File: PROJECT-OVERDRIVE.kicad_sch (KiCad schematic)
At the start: 57 parts, among them J1 PJ-327A0-SMT, J2 USB_C_Receptacle_USB2.0_16P, K1 G6S-2, P1 SSD1306_ribbon, U1 CH32V30xVxTx, U2 PCM5102APWR, U3 MAX4410EUD+, U4 AP2112K-3.3, U5 AP2112K-3.3, U6 LM324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

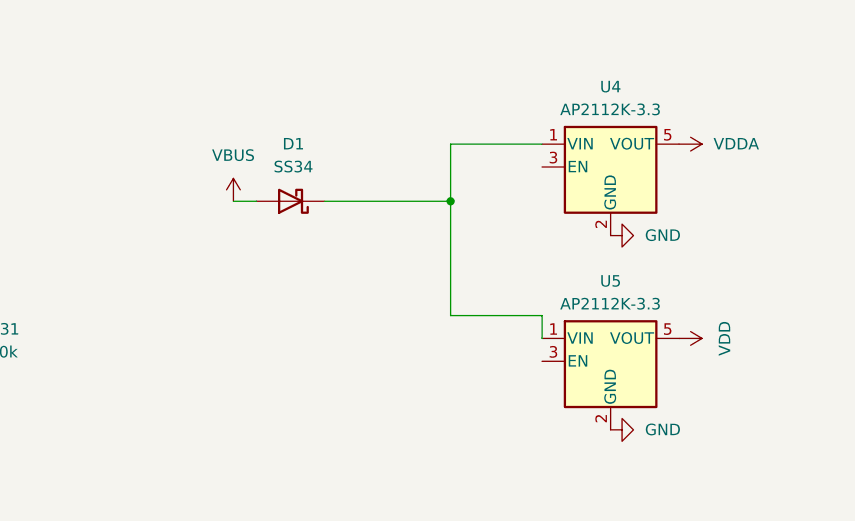
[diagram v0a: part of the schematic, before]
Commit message: Add fuses
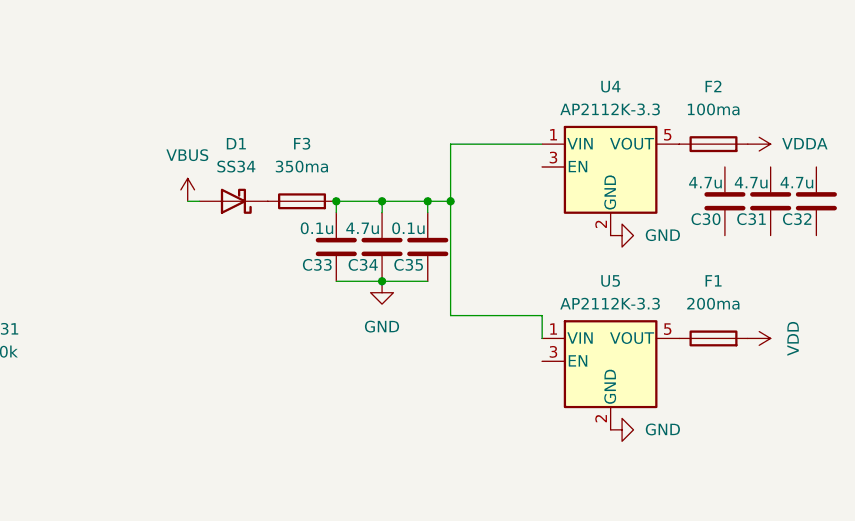
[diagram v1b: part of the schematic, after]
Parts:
- added C30, C31, C32, C34: 4.7u, Capacitor_SMD:C_0805_2012Metric, symbol Device:C
- added C33, C35: 0.1u, Capacitor_SMD:C_0805_2012Metric, symbol Device:C
- added F1: 200ma, Fuse:Fuse_0805_2012Metric, symbol Device:Fuse
- added F2: 100ma, Fuse:Fuse_0805_2012Metric, symbol Device:Fuse
- added F3: 350ma, Fuse:Fuse_0805_2012Metric, symbol Device:Fuse
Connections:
- net GND: now also C33.2, C34.2, C35.2
- net VDD: now also F1.2; no longer U5.5 (VOUT)
- net VDDA: now also F2.2; no longer U4.5 (VOUT)
- net at U4.1 (VIN), U5.1 (VIN): now also C33.1, C34.1, C35.1, F3.2; no longer D1.1 (K)
- new net: F2.1, U4.5 (VOUT)
- new net: D1.1 (K), F3.1
- new net: F1.1, U5.5 (VOUT)
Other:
- moved on the sheet: D1

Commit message: finished power supply section
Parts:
- added C36, C37: 4.7u, Capacitor_SMD:C_0805_2012Metric, symbol Device:C
- added C38: 0.1u, Capacitor_SMD:C_0805_2012Metric, symbol Device:C
- added Q1, Q2: AO3401A, Package_TO_SOT_SMD:SOT-23, symbol Transistor_FET:AO3401A
- added R10, R9: 1k, Resistor_SMD:R_0805_2012Metric_Pad1.20x1.40mm_HandSolder, symbol Device:R
- added R11, R12: 10k, Resistor_SMD:R_0805_2012Metric_Pad1.20x1.40mm_HandSolder, symbol Device:R
- C32: value 4.7u -> 0.1u
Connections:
- net +3.3VA: now also Q2.3 (D); no longer U6.3 (+), U6.5 (+)
- net +3.3VDAC: now also Q1.3 (D)
- net GND: now also C30.2, C31.2, C32.2, C36.2, C37.2, C38.2
- net VDDA: now also U6.3 (+), U6.5 (+), Q1.2 (S), Q2.2 (S), R11.2, R12.2
- net at F2.1, U4.5 (VOUT): now also C30.1, C31.1, C32.1
- net at F1.1, U5.5 (VOUT): now also C36.1, C37.1, C38.1
- new net: Q2.1 (G), R10.2, R11.1
- new net: Q1.1 (G), R12.1, R9.2
- new net VAMP_EN: R10.1
- new net VDAC_EN: R9.1
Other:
- note added: "POWER"

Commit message: added exp port(to be finished)
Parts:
- added F4: 250ma, Fuse:Fuse_0805_2012Metric, symbol Device:Fuse
- added J3: Conn_02x10_Odd_Even, symbol Connector_Generic:Conn_02x10_Odd_Even
- added Q3: S8050, Package_TO_SOT_THT:TO-92_Inline, symbol Transistor_BJT:S8050
- added RN1, RN2: 22, Resistor_SMD:R_Array_Concave_4x0603, symbol Device:R_Pack04
- F3: value 350ma -> 250ma
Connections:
- net DAC_BCK: now also RN1.8 (R1.2)
- net DAC_MUTE: now also U1.53 (PB14)
- net GND: now also Q3.1 (E)
- net +5V: now reaches K1.1
- net +5V: now also C33.1, C34.1, C35.1, F3.2, U4.1 (VIN), U5.1 (VIN)
- net at K1.12: now also Q3.3 (C)
- net at D1.1 (K), F3.1: now also F4.2
- net EXP_I2S_LRCLK: now reaches U1.77 (PA15)
- net EXP_I2S_LRCLK: now also RN1.7 (R2.2)
- net EXP_I2S_CLK: now reaches U1.89 (PB3)
- net EXP_I2S_CLK: now also RN1.6 (R3.2)
- net EXP_I2S_SD: now reaches U1.91 (PB5)
- net EXP_I2S_SD: now also RN1.5 (R4.2)
- new net: J3.10 (Pin_10), RN2.8 (R1.2)
- new net: J3.3 (Pin_3), RN1.4 (R4.1)
- new net: J3.4 (Pin_4), RN2.5 (R4.2)
- new net: J3.5 (Pin_5), RN1.3 (R3.1)
- new net: J3.6 (Pin_6), RN2.6 (R3.2)
- new net: J3.7 (Pin_7), RN1.2 (R2.1)
- new net: J3.8 (Pin_8), RN2.7 (R2.2)
- new net: J3.9 (Pin_9), RN1.1 (R1.1)
- new net +5VP: F4.1

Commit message: expansion port mostly finished(TODO:Add some gpios to there) relay circuit finished(need to connect to mcu)
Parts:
- removed RN1: 22, Resistor_SMD:R_Array_Concave_4x0603, symbol Device:R_Pack04
- added R13, R14, R15: 22r, Resistor_SMD:R_0603_1608Metric, symbol Device:R
- added R16: 1k, Resistor_SMD:R_0805_2012Metric, symbol Device:R
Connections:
- net +5VP: now also J3.1 (Pin_1), J3.2 (Pin_2)
- net DAC_BCK: now also J3.6 (Pin_6), RN2.6 (R3.2); no longer U1.52 (PB13), U2.13 (BCK)
- net DAC_DIN: now also J3.4 (Pin_4), RN2.8 (R1.2); no longer U1.54 (PB15), U2.14 (DIN)
- net DAC_LRCLK: now also J3.8 (Pin_8), RN2.5 (R4.2); no longer U1.51 (PB12), U2.15 (LRCK)
- net DAC_MUTE: now also J3.10 (Pin_10), RN2.7 (R2.2); no longer U1.53 (PB14)
- net EXP_I2S_CLK: now also J3.5 (Pin_5), R14.1; no longer U1.89 (PB3)
- net EXP_I2S_LRCLK: now also J3.7 (Pin_7), R13.1; no longer U1.77 (PA15)
- net EXP_I2S_SD: now also J3.3 (Pin_3), R15.1; no longer U1.91 (PB5)
- net GND: now also J3.19 (Pin_19), J3.20 (Pin_20)
- net I2C_SCL: now reaches J3.15 (Pin_15)
- net I2C_SCL: now also U1.47 (PB10)
- net I2C_SDA: now reaches J3.17 (Pin_17)
- net I2C_SDA: now also U1.48 (PB11)
- net at RN2.1 (R1.1): now also U1.54 (PB15)
- net at RN2.2 (R2.1): now also U1.53 (PB14)
- net at RN2.3 (R3.1): now also U1.52 (PB13)
- net at RN2.4 (R4.1): now also U1.51 (PB12)
- net at Q3.2 (B): now also R16.2
- new net: R13.2, U1.77 (PA15)
- new net: R14.2, U1.89 (PB3)
- new net: R15.2, U1.91 (PB5)
- new net RELAY_TOGGLE: R16.1
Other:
- moved on the sheet: RN2

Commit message: idkmyinternetwasdead.git
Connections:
- net DAC_BCK: now also U2.13 (BCK)
- net DAC_DIN: now also U2.14 (DIN)
- net DAC_LRCLK: now also U2.15 (LRCK)
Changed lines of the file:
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@@
 	(global_label "DAC_LRCLK"
 		(shape input)
-		(at 170.561 91.059 270)
-		(fields_autoplaced yes)
-		(effects
-			(font
-				(size 1.27 1.27)
-			)
-			(justify right)
-		)
-		(property "Intersheetrefs" "${INTERSHEET_REFS}"
-			(at 170.561 104.5066 90)
+		(at 166.37 95.25 180)
+		(fields_autoplaced yes)
+		(effects
+			(font
+				(size 1.27 1.27)
+			)
+			(justify right)
+		)
+		(property "Intersheetrefs" "${INTERSHEET_REFS}"
+			(at 152.9224 95.25 0)
 			(effects
 				(font
@@
 	(global_label "DAC_DIN"
 		(shape input)
-		(at 162.941 91.059 270)
-		(fields_autoplaced yes)
-		(effects
-			(font
-				(size 1.27 1.27)
-			)
-			(justify right)
-		)
-		(property "Intersheetrefs" "${INTERSHEET_REFS}"
-			(at 162.941 101.8457 90)
+		(at 166.37 87.63 180)
+		(fields_autoplaced yes)
+		(effects
+			(font
+				(size 1.27 1.27)
+			)
+			(justify right)
+		)
+		(property "Intersheetrefs" "${INTERSHEET_REFS}"
+			(at 155.5833 87.63 0)
 			(effects
 				(font
@@
 	(global_label "DAC_BCK"
 		(shape input)
-		(at 165.481 91.059 270)
-		(fields_autoplaced yes)
-		(effects
-			(font
-				(size 1.27 1.27)
-			)
-			(justify right)
-		)
-		(property "Intersheetrefs" "${INTERSHEET_REFS}"
-			(at 165.481 102.4504 90)
-			(effects
-				(font
+		(at 166.37 90.17 180)
+		(fields_autoplaced yes)
+		(effects
+			(font
+				(size 1.27 1.27)
+			)
+			(justify right)
+		)
+		(property "Intersheetrefs" "${INTERSHEET_REFS}"
+			(at 154.9786 90.17 0)
+			(effects
+				(font

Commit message: fixed up op amp connection
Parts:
- added R17, R18, R19: 10k, Resistor_SMD:R_0805_2012Metric, symbol Device:R
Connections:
- net GND: now also R18.1
- net VDDA: now also R17.1, R19.2; no longer U6.3 (+)
- net at J1.6, U6.2 (-): now also R19.1
- new net: R17.2, R18.2, U6.3 (+)

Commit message: idk
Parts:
- added R20: 100k, Resistor_SMD:R_0805_2012Metric, symbol Device:R
- R19: value 10k -> 100k
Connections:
- net at J1.6, R19.1: now also R20.2; no longer U6.2 (-)
- new net: R20.1, U6.2 (-)
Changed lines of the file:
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@@
 	)
 	(junction
+		(at 259.08 119.38)
+		(diameter 0)
+		(color 0 0 0 0)
+	)
+	(junction
 		(at 248.92 52.324)
 		(diameter 0)
@@
 	)
 	(junction
-		(at 259.08 119.38)
-		(diameter 0)
-		(color 0 0 0 0)
-	)
-	(junction
 		(at 142.24 30.48)
 		(diameter 0)
@@
 	(wire
 		(pts
-			(xy 259.08 132.08) (xy 256.54 132.08)
+			(xy 60.96 193.04) (xy 68.58 193.04)
 		)
 		(stroke
 			(width 0)
 			(type default)
-			(color 255 255 0 1)
 		)
 	)
 	(wire
 		(pts
-			(xy 60.96 193.04) (xy 68.58 193.04)
+			(xy 43.18 24.13) (xy 48.26 24.13)
 		)
 		(stroke
@@
 	(wire
 		(pts
-			(xy 43.18 24.13) (xy 48.26 24.13)
+			(xy 63.5 31.75) (xy 68.58 31.75)
 		)
 		(stroke
@@
 	(wire
 		(pts
-			(xy 63.5 31.75) (xy 68.58 31.75)
+			(xy 340.36 34.29) (xy 345.44 34.29)
 		)
 		(stroke
@@
 	(wire
 		(pts
-			(xy 340.36 34.29) (xy 345.44 34.29)
+			(xy 250.952 49.784) (xy 249.936 49.784)
 		)
 		(stroke
@@
 	(wire
 		(pts
-			(xy 250.952 49.784) (xy 249.936 49.784)
+			(xy 259.08 119.38) (xy 259.08 124.46)
 		)
 		(stroke
@@
 	(wire
 		(pts
+			(xy 259.08 132.08) (xy 256.54 132.08)
+		)
+		(stroke
+			(width 0)
+			(type default)
+			(color 255 255 0 1)
+		)
+	)
+	(wire
+		(pts
 			(xy 85.09 40.64) (xy 85.09 41.91)
 		)
@@
 	(wire
 		(pts
-			(xy 259.08 119.38) (xy 259.08 132.08)
-		)
-		(stroke
-			(width 0)
-			(type default)
-			(color 255 255 0 1)
-		)
-	)
-	(wire
-		(pts
 			(xy 246.38 95.25) (xy 238.76 95.25)
 		)
@@
 		(dnp no)
 		(property "Reference" "R18"
-			(at 261.62 128.778 90)
+			(at 265.176 125.222 90)
 			(effects
 				(font
@@
 			)
 		)
-		(property "Value" "10k"
+		(property "Value" "100k"
 			(at 267.97 115.57 90)
 			(effects
@@
 					(unit 1)
 				)
+			)
+		)
+	)
+	(symbol
+		(lib_id "Device:R")
+		(at 259.08 128.27 180)
+		(unit 1)
+		(exclude_from_sim no)
+		(in_bom yes)
+		(on_board yes)
+		(dnp no)
+		(property "Reference" "R20"
+			(at 256.794 133.096 0)
+			(effects
+				(font
+					(size 1.27 1.27)
+				)
+				(justify right)
+			)
+		)
+		(property "Value" "100k"
+			(at 260.604 130.048 0)
+			(effects
+				(font
+					(size 1.27 1.27)
+				)
+				(justify right)
+			)
+		)
+		(property "Footprint" "Resistor_SMD:R_0805_2012Metric"
+			(at 260.858 128.27 90)
+			(effects
+				(font
+					(size 1.27 1.27)
+				)
+				(hide yes)
+			)
+		)
+		(property "Datasheet" "~"
+			(at 259.08 128.27 0)
+			(effects
+				(font
+					(size 1.27 1.27)
+				)
+				(hide yes)
+			)
+		)
+		(property "Description" "Resistor"
+			(at 259.08 128.27 0)
+			(effects
+				(font
+					(size 1.27 1.27)
+				)
+				(hide yes)
+			)
+		)
+		(pin "2"
+		)
+		(pin "1"
+		)
+		(instances
+			(project "PROJECT-OVERDRIVE"
+				(path "/265f6b68-58df-43b8-965c-fef7b735041c"
+					(reference "R20")
+					(unit 1)
+				)

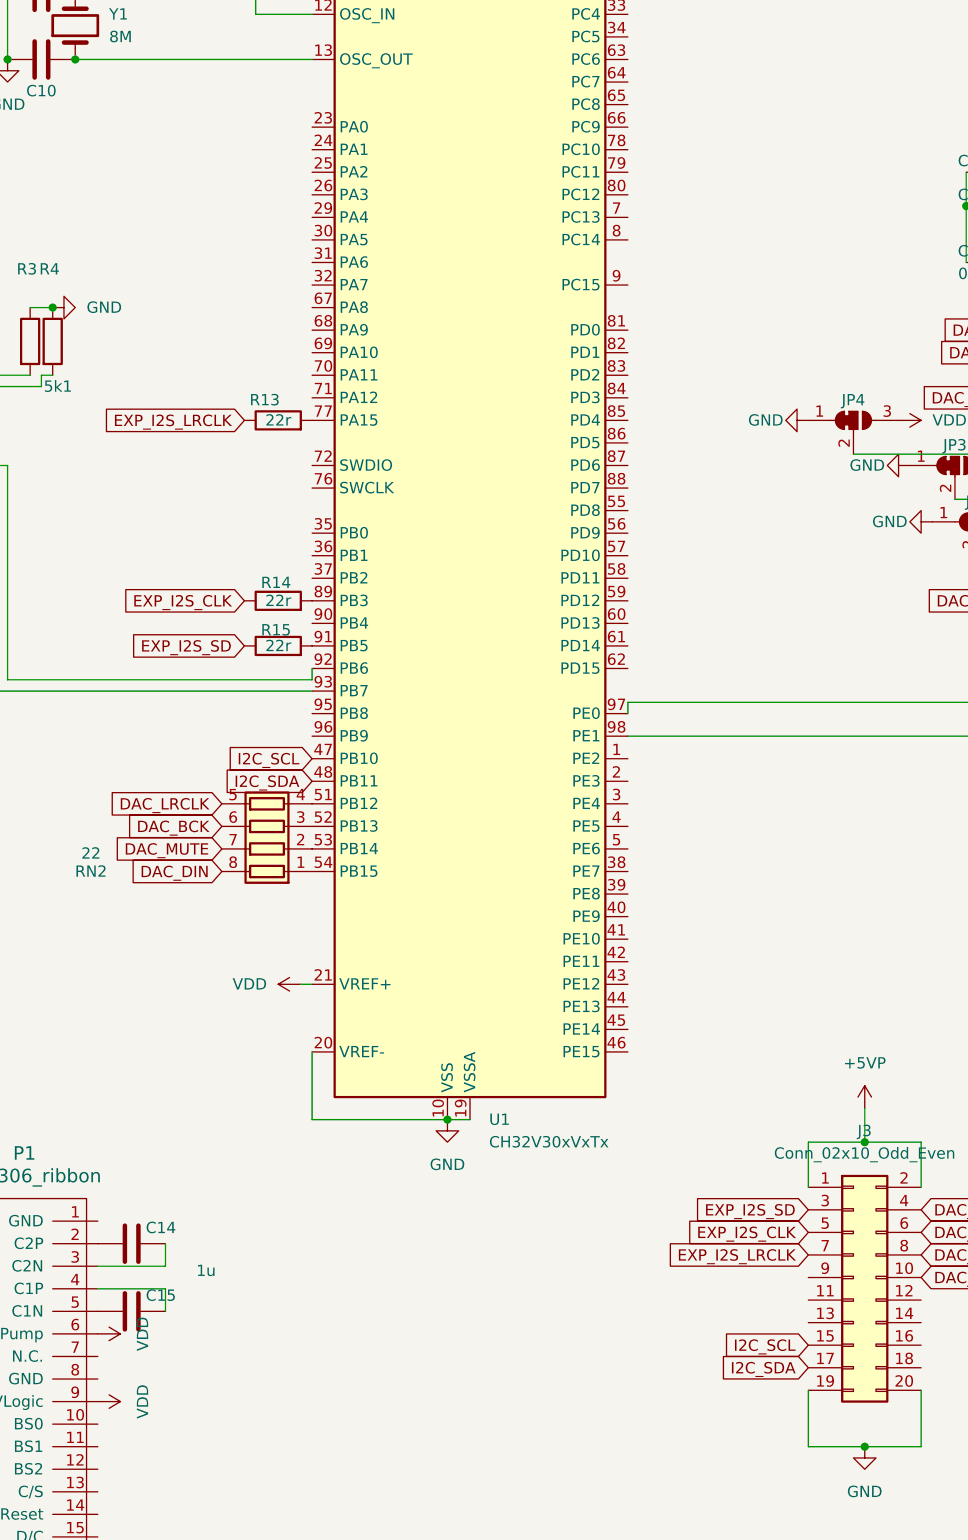
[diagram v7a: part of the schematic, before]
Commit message: Add some connections to the mcu
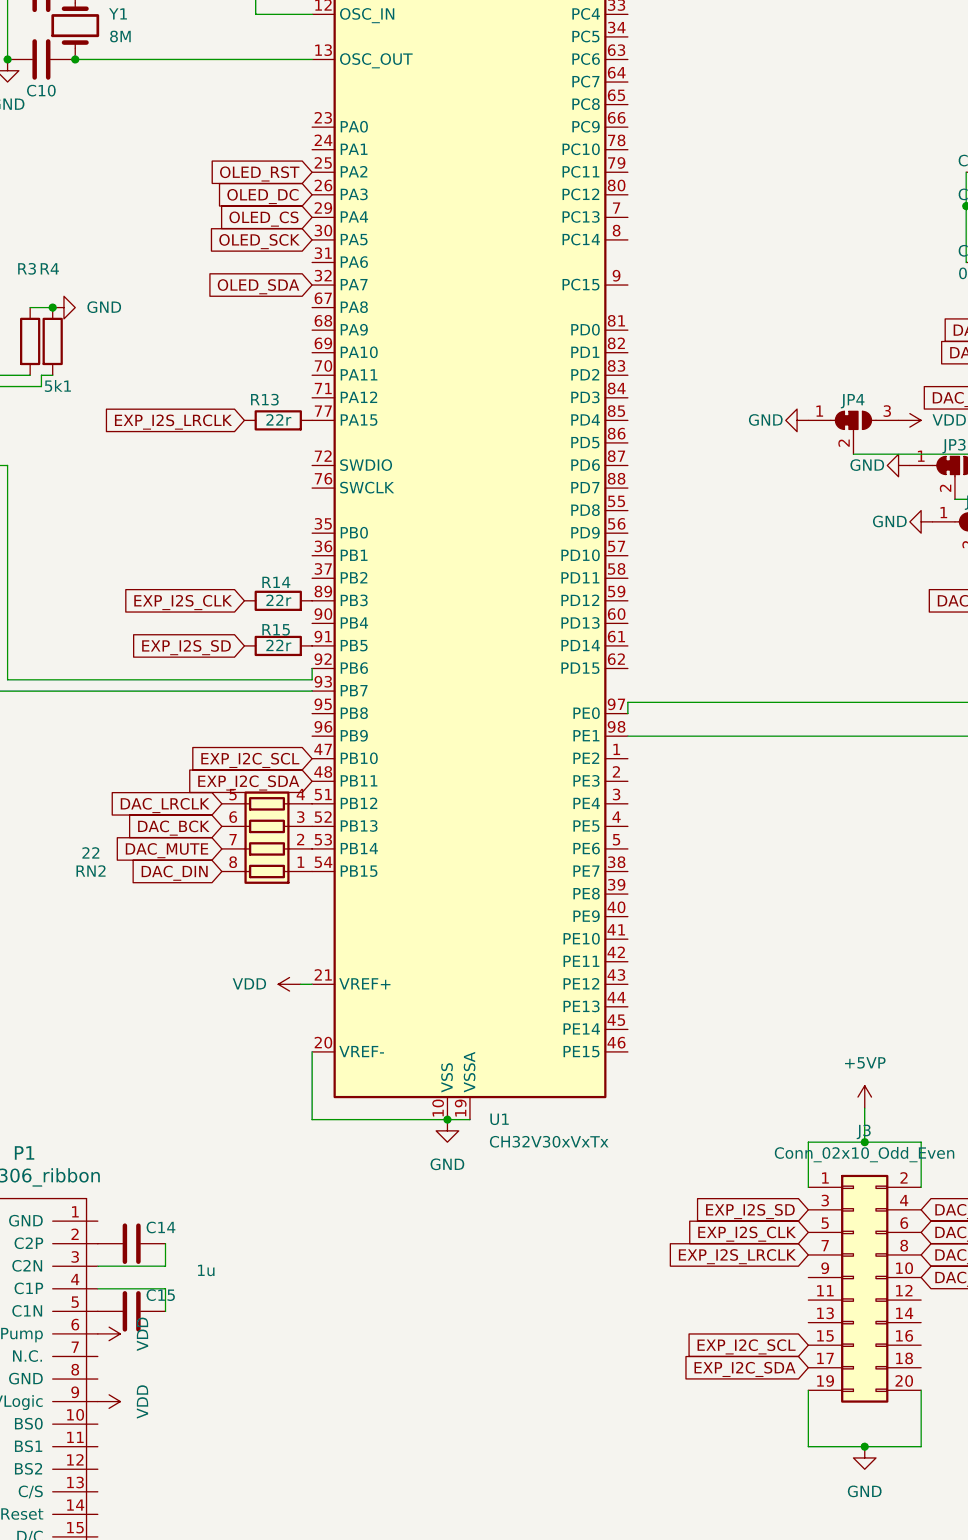
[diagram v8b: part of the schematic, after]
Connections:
- net OLED_RST: now reaches U1.25 (PA2)
- net OLED_DC: now reaches U1.26 (PA3)
- net OLED_CS: now reaches U1.29 (PA4)
- net OLED_SCK: now reaches U1.30 (PA5)
- net OLED_SDA: now reaches U1.32 (PA7)
- net I2C_SCL renamed EXP_I2C_SCL
- net I2C_SDA renamed EXP_I2C_SDA
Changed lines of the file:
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@@
+		)
+	)
+	(global_label "OLED_RST"
+		(shape input)
+		(at 85.09 69.85 180)
+		(fields_autoplaced yes)
+		(effects
+			(font
+				(size 1.27 1.27)
+			)
+			(justify right)
+		)
+		(property "Intersheetrefs" "${INTERSHEET_REFS}"
+			(at 72.9125 69.85 0)
+			(effects
+				(font
+					(size 1.27 1.27)
+				)
+				(justify right)
+				(hide yes)
+			)
 		)
 	)
@@
 		)
 	)
-	(global_label "I2C_SDA"
+	(global_label "EXP_I2C_SDA"
 		(shape input)
 		(at 85.09 138.43 180)
@@
 		)
 		(property "Intersheetrefs" "${INTERSHEET_REFS}"
-			(at 74.4848 138.43 0)
+			(at 69.8887 138.43 0)
 			(effects
 				(font
@@
 		)
 	)
-	(global_label "I2C_SCL"
+	(global_label "EXP_I2C_SCL"
 		(shape input)
 		(at 140.97 201.93 180)
@@
 		)
 		(property "Intersheetrefs" "${INTERSHEET_REFS}"
-			(at 130.4253 201.93 0)
+			(at 125.8292 201.93 0)
+			(effects
+				(font
+					(size 1.27 1.27)
+				)
+				(justify right)
+				(hide yes)
+			)
+		)
+	)
+	(global_label "OLED_CS"
+		(shape input)
+		(at 85.09 74.93 180)
+		(fields_autoplaced yes)
+		(effects
+			(font
+				(size 1.27 1.27)
+			)
+			(justify right)
+		)
+		(property "Intersheetrefs" "${INTERSHEET_REFS}"
+			(at 73.8801 74.93 0)
+			(effects
+				(font
+					(size 1.27 1.27)
+				)
+				(justify right)
+				(hide yes)
+			)
+		)
+	)
+	(global_label "OLED_SCK"
+		(shape input)
+		(at 85.09 77.47 180)
+		(fields_autoplaced yes)
+		(effects
+			(font
+				(size 1.27 1.27)
+			)
+			(justify right)
+		)
+		(property "Intersheetrefs" "${INTERSHEET_REFS}"
+			(at 72.6101 77.47 0)
+			(effects
+				(font
+					(size 1.27 1.27)
+				)
+				(justify right)
+				(hide yes)
+			)
+		)
+	)
+	(global_label "OLED_SDA"
+		(shape input)
+		(at 85.09 82.55 180)
+		(fields_autoplaced yes)
+		(effects
+			(font
+				(size 1.27 1.27)
+			)
+			(justify right)
+		)
+		(property "Intersheetrefs" "${INTERSHEET_REFS}"
+			(at 72.7915 82.55 0)
 			(effects
 				(font
@@
 		)
 	)
-	(global_label "I2C_SCL"
+	(global_label "EXP_I2C_SCL"
 		(shape input)
 		(at 85.09 135.89 180)
@@
 		)
 		(property "Intersheetrefs" "${INTERSHEET_REFS}"
-			(at 74.5453 135.89 0)
+			(at 69.9492 135.89 0)
 			(effects
 				(font
@@
 		)
 	)
-	(global_label "I2C_SDA"
+	(global_label "OLED_DC"
+		(shape input)
+		(at 85.09 72.39 180)
+		(fields_autoplaced yes)
+		(effects
+			(font
+				(size 1.27 1.27)
+			)
+			(justify right)
+		)
+		(property "Intersheetrefs" "${INTERSHEET_REFS}"
+			(at 73.8196 72.39 0)
+			(effects
+				(font
+					(size 1.27 1.27)
+				)
+				(justify right)
+				(hide yes)
+			)
+		)
+	)
+	(global_label "EXP_I2C_SDA"
 		(shape input)
 		(at 140.97 204.47 180)
@@
 		)
 		(property "Intersheetrefs" "${INTERSHEET_REFS}"
-			(at 130.3648 204.47 0)
-			(effects
-				(font
+			(at 125.7687 204.47 0)
+			(effects
+				(font
